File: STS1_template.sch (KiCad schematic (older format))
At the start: 10 parts, among them J1 Conn_01x02_Female, U1 coordinate_system

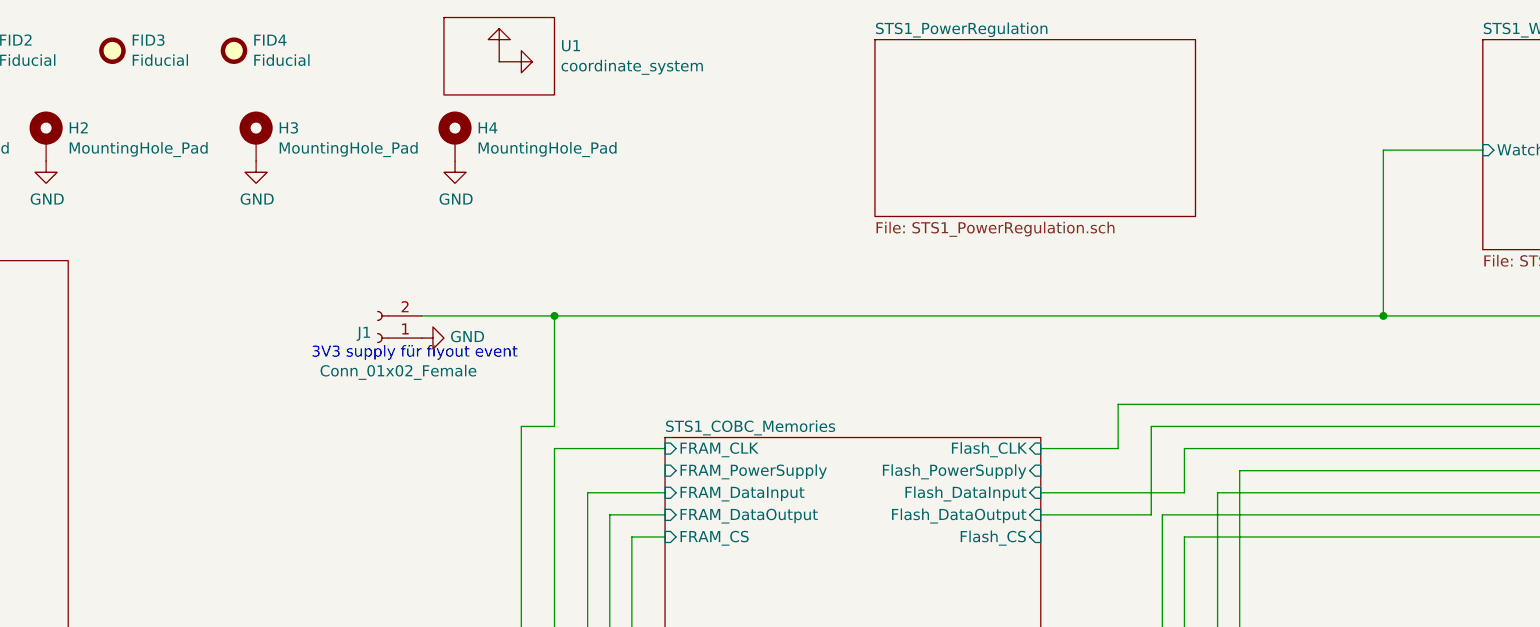
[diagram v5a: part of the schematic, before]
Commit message: BuckBoost added
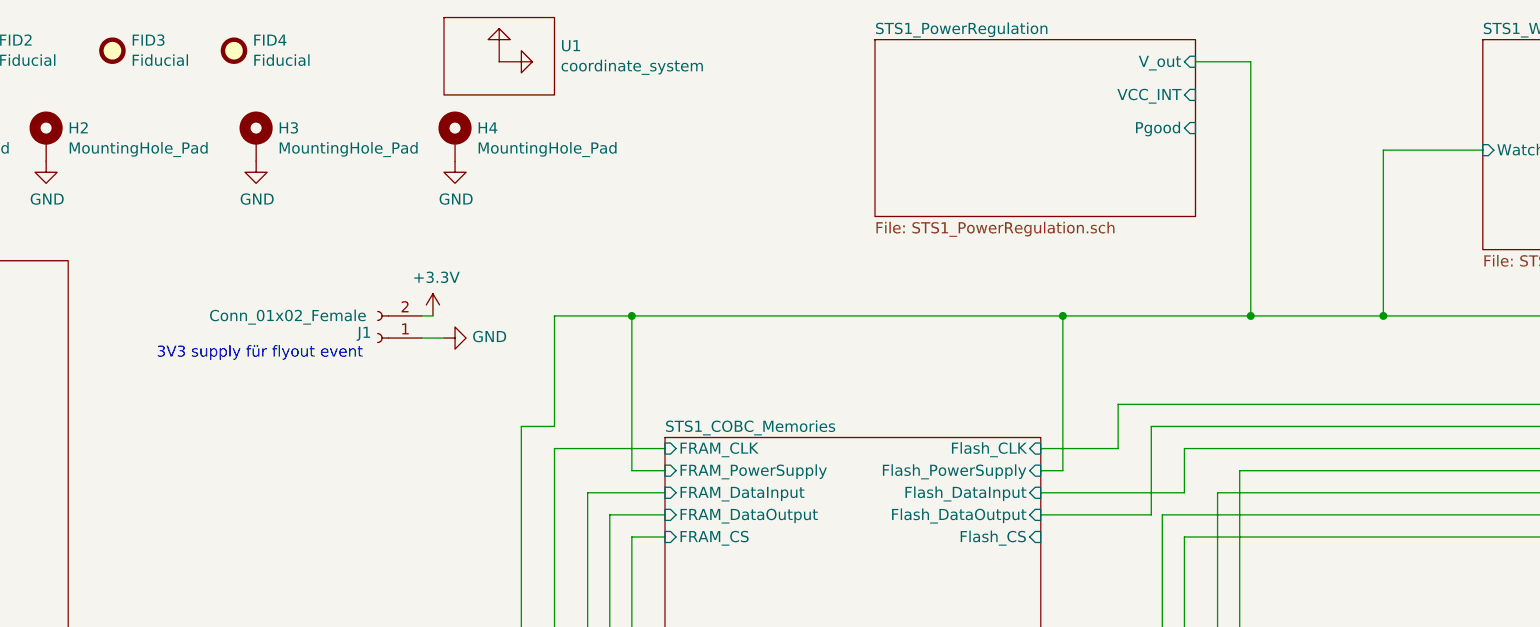
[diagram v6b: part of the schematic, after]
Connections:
- net STS1_COBC_uC/STM32_PowerSupply1 renamed +3V3
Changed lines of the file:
@@
 F5 "Flash_DataOutput" I R 6100 2800 50
 F6 "Flash_CS" I R 6100 2900 50
-F7 "FRAM_CS" I L 4400 2900 50
-F8 "FRAM_CLK" I L 4400 2500 50
-F9 "FRAM_DataInput" I L 4400 2700 50
-F10 "FRAM_DataOutput" I L 4400 2800 50
-F11 "FRAM_PowerSupply" I L 4400 2600 50
+F7 "FRAM_CLK" I L 4400 2500 50
+F8 "FRAM_DataInput" I L 4400 2700 50
+F9 "FRAM_DataOutput" I L 4400 2800 50
+F10 "FRAM_PowerSupply" I L 4400 2600 50
+F11 "FRAM_CS" I L 4400 2900 50
 $EndSheet
 Wire Wire Line
@@
 	8950 2900 6750 2900
 Wire Wire Line
-	6750 2900 6750 3900
-Wire Wire Line
 	6750 3900 3900 3900
 Wire Wire Line
@@
 Wire Wire Line
 	8950 2700 6900 2700
-Wire Wire Line
-	6900 2700 6900 3700
 Wire Wire Line
 	6900 3700 4150 3700
@@
 F0 "STS1_PowerRegulation" 50
 F1 "STS1_PowerRegulation.sch" 50
+F2 "V_out" I R 6800 750 50
+F3 "VCC_INT" I R 6800 900 50
+F4 "Pgood" I R 6800 1050 50
 $EndSheet
 $Sheet
@@
 P 3100 2000
 F 0 "J1" H 3128 1976 50  0000 L CNN
-F 1 "Conn_01x02_Female" H 2650 2150 50  0000 L CNN
+F 1 "Conn_01x02_Female" H 3150 1900 50  0000 L CNN
 F 2 "Connector_PinHeader_2.54mm:PinHeader_1x02_P2.54mm_Vertical" H 3100 2000 50  0001 C CNN
 F 3 "~" H 3100 2000 50  0001 C CNN
@@
 	-1   0    0    1
 $EndComp
-Text Notes 2800 2100 0    50   ~ 0
+Text Notes 2100 2100 0    50   ~ 0
 3V3 supply für flyout event\n
 Wire Wire Line
-	3300 1900 3900 1900
+	3300 1900 3350 1900
 Wire Wire Line
 	8600 1900 8600 3100
@@
 L power:GND #PWR0123
 U 1 1 612FF8A3
-P 3300 2000
-F 0 "#PWR0123" H 3300 1750 50  0001 C CNN
-F 1 "GND" V 3305 1872 50  0000 R CNN
-F 2 "" H 3300 2000 50  0001 C CNN
-F 3 "" H 3300 2000 50  0001 C CNN
-	1    3300 2000
+P 3400 2000
+F 0 "#PWR0123" H 3400 1750 50  0001 C CNN
+F 1 "GND" V 3405 1872 50  0000 R CNN
+F 2 "" H 3400 2000 50  0001 C CNN
+F 3 "" H 3400 2000 50  0001 C CNN
+	1    3400 2000
 	0    -1   -1   0
 $EndComp
@@
 Wire Wire Line
 	3750 6100 2600 6100
-Connection ~ 3900 1900
-Wire Wire Line
-	3900 1900 7650 1900
 Wire Wire Line
 	3750 5900 550  5900
@@
 	8950 2600 7000 2600
 Wire Wire Line
-	7000 2600 7000 3600
-Wire Wire Line
 	7000 3600 4250 3600
 Wire Wire Line
@@
 Wire Wire Line
 	10400 1050 10100 1050
+Wire Wire Line
+	7000 2600 7000 3600
+Wire Wire Line
+	6900 2700 6900 3700
+Wire Wire Line
+	6750 2900 6750 3900
+$Comp
+L power:+3.3V #PWR0157
+U 1 1 615E09EC
+P 3350 1900
+F 0 "#PWR0157" H 3350 1750 50  0001 C CNN
+F 1 "+3.3V" H 3365 2073 50  0000 C CNN
+F 2 "" H 3350 1900 50  0001 C CNN
+F 3 "" H 3350 1900 50  0001 C CNN
+	1    3350 1900
+	1    0    0    -1
+$EndComp
+Wire Wire Line
+	3300 2000 3400 2000
+Wire Wire Line
+	6800 750  7050 750
+Wire Wire Line
+	7050 750  7050 1900
+Connection ~ 7050 1900
+Wire Wire Line
+	7050 1900 7650 1900
+Wire Wire Line
+	4400 2600 4250 2600
+Wire Wire Line
+	4250 2600 4250 1900
+Wire Wire Line
+	3900 1900 4250 1900
+Connection ~ 4250 1900
+Wire Wire Line
+	4250 1900 6200 1900
+Wire Wire Line
+	6100 2600 6200 2600
+Wire Wire Line
+	6200 2600 6200 1900
+Connection ~ 6200 1900
+Wire Wire Line
+	6200 1900 7050 1900
 $EndSCHEMATC

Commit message: schematic done
final tweaks (adding LEDS, pin headers, moving circuits...)
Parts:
- removed J1: Conn_01x02_Female, Connector_PinHeader_2.54mm:PinHeader_1x02_P2.54mm_Vertical, symbol Connector:Conn_01x02_Female
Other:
- note removed: "3V3 supply für flyout event\n"

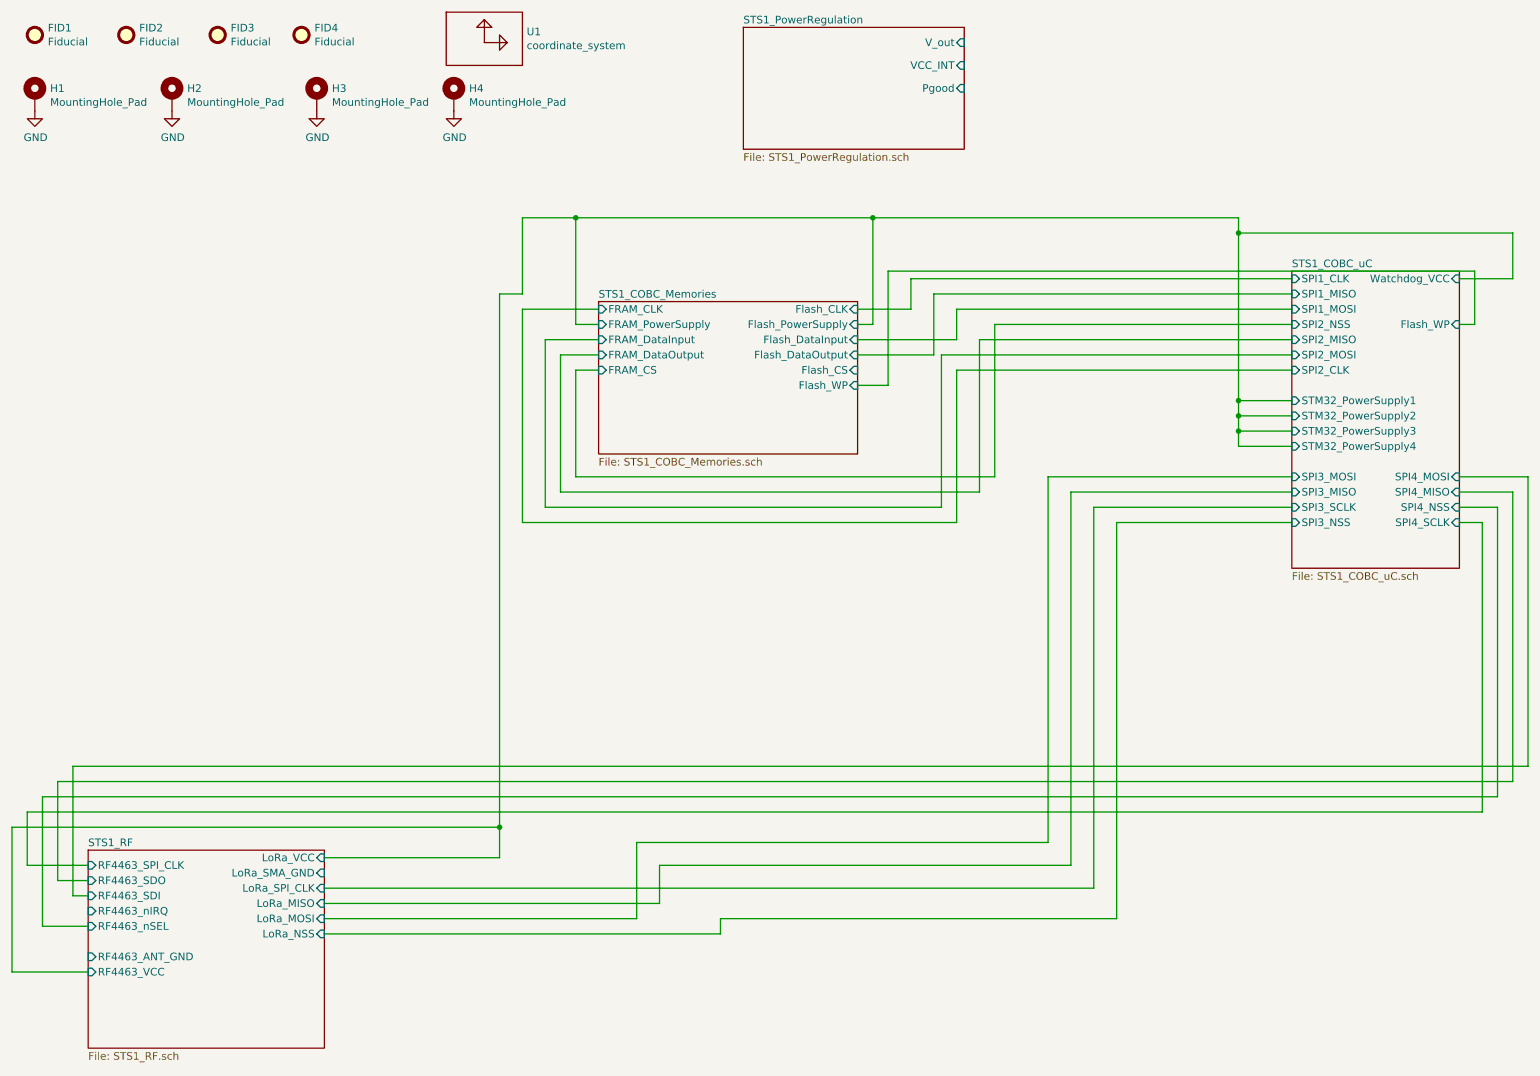
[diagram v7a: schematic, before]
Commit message: Issues removed + further layout development
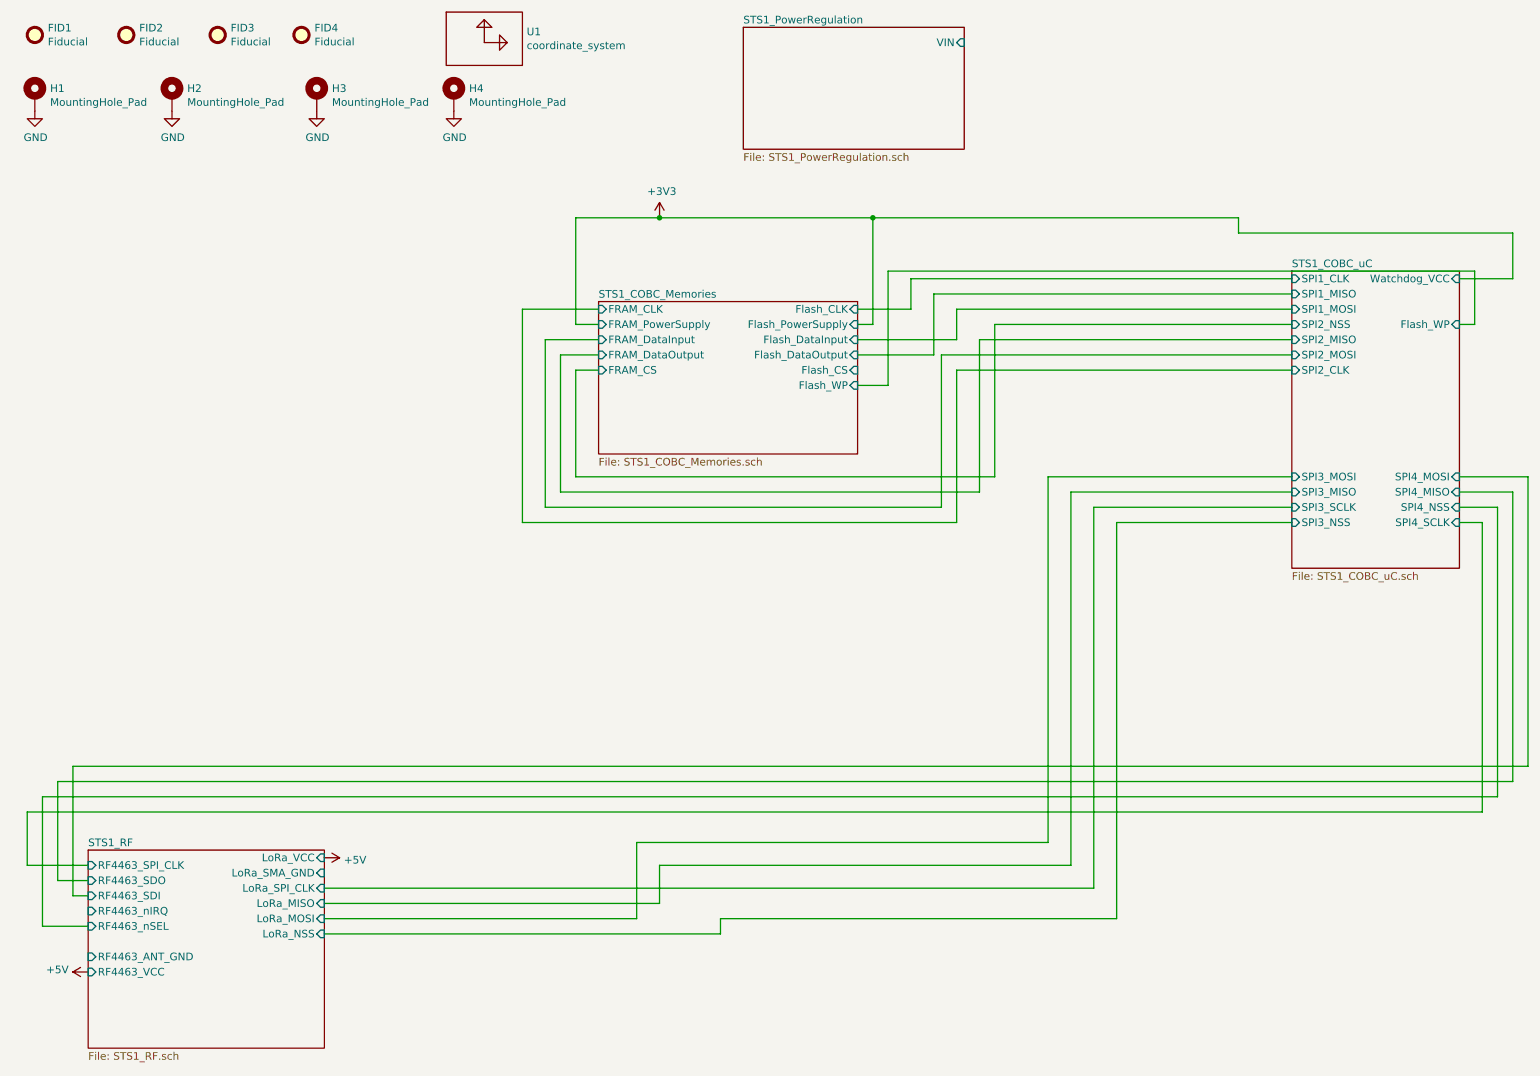
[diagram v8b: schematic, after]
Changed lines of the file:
@@
 Wire Wire Line
 	4150 2800 4400 2800
-$Sheet
-S 5350 650  1450 800
-U 61293CFB
-F0 "STS1_PowerRegulation" 50
-F1 "STS1_PowerRegulation.sch" 50
-F2 "V_out" I R 6800 750 50
-F3 "VCC_INT" I R 6800 900 50
-F4 "Pgood" I R 6800 1050 50
-$EndSheet
 Wire Wire Line
 	8600 1900 8600 2000
-Wire Wire Line
-	8600 3100 8950 3100
 $Sheet
 S 1050 6050 1550 1300
@@
 	7350 3600 8950 3600
 Wire Wire Line
-	3900 1900 3900 2400
-Wire Wire Line
-	3900 2400 3750 2400
-Wire Wire Line
-	3750 2400 3750 5900
-Wire Wire Line
-	3750 6100 2600 6100
-Wire Wire Line
-	3750 5900 550  5900
-Wire Wire Line
-	550  5900 550  6850
-Wire Wire Line
-	550  6850 1050 6850
-Connection ~ 3750 5900
-Wire Wire Line
-	3750 5900 3750 6100
-Wire Wire Line
-	8600 3100 8600 3200
-Wire Wire Line
-	8600 3200 8950 3200
-Connection ~ 8600 3100
-Wire Wire Line
-	8600 3200 8600 3300
-Wire Wire Line
-	8600 3300 8950 3300
-Connection ~ 8600 3200
-Wire Wire Line
-	8600 3300 8600 3400
-Wire Wire Line
-	8600 3400 8950 3400
-Connection ~ 8600 3300
-Wire Wire Line
 	10050 3900 10200 3900
 Wire Wire Line
@@
 	4250 2600 4250 1900
 Wire Wire Line
-	3900 1900 4250 1900
-Connection ~ 4250 1900
-Wire Wire Line
-	4250 1900 6200 1900
+	4250 1900 4800 1900
 Wire Wire Line
 	6100 2600 6200 2600
@@
 Wire Wire Line
 	6200 1900 8600 1900
+Wire Wire Line
+	10050 2300 10400 2300
+Wire Wire Line
+	10400 2300 10400 2000
+Wire Wire Line
+	10400 2000 8600 2000
 $Sheet
 S 8950 2250 1100 1950
@@
 F6 "SPI2_MOSI" I L 8950 2800 50
 F7 "SPI2_CLK" I L 8950 2900 50
-F8 "STM32_PowerSupply1" I L 8950 3100 50
-F9 "STM32_PowerSupply2" I L 8950 3200 50
-F10 "STM32_PowerSupply3" I L 8950 3300 50
-F11 "STM32_PowerSupply4" I L 8950 3400 50
-F12 "SPI3_MOSI" I L 8950 3600 50
-F13 "SPI3_MISO" I L 8950 3700 50
-F14 "SPI3_SCLK" I L 8950 3800 50
-F15 "SPI3_NSS" I L 8950 3900 50
-F16 "SPI4_MOSI" I R 10050 3600 50
-F17 "SPI4_MISO" I R 10050 3700 50
-F18 "SPI2_NSS" I L 8950 2600 50
-F19 "SPI4_NSS" I R 10050 3800 50
-F20 "SPI4_SCLK" I R 10050 3900 50
-F21 "Flash_WP" I R 10050 2600 50
-F22 "Watchdog_VCC" I R 10050 2300 50
+F8 "SPI3_MOSI" I L 8950 3600 50
+F9 "SPI3_MISO" I L 8950 3700 50
+F10 "SPI3_SCLK" I L 8950 3800 50
+F11 "SPI3_NSS" I L 8950 3900 50
+F12 "SPI4_MOSI" I R 10050 3600 50
+F13 "SPI4_MISO" I R 10050 3700 50
+F14 "SPI2_NSS" I L 8950 2600 50
+F15 "SPI4_NSS" I R 10050 3800 50
+F16 "SPI4_SCLK" I R 10050 3900 50
+F17 "Flash_WP" I R 10050 2600 50
+F18 "Watchdog_VCC" I R 10050 2300 50
 $EndSheet
-Wire Wire Line
-	10050 2300 10400 2300
-Wire Wire Line
-	10400 2300 10400 2000
-Wire Wire Line
-	10400 2000 8600 2000
-Connection ~ 8600 2000
-Wire Wire Line
-	8600 2000 8600 3100
+$Comp
+L power:+3V3 #PWR0105
+U 1 1 617A5044
+P 4800 1900
+F 0 "#PWR0105" H 4800 1750 50  0001 C CNN
+F 1 "+3V3" H 4815 2073 50  0000 C CNN
+F 2 "" H 4800 1900 50  0001 C CNN
+F 3 "" H 4800 1900 50  0001 C CNN
+	1    4800 1900
+	1    0    0    -1
+$EndComp
+Connection ~ 4800 1900
+Wire Wire Line
+	4800 1900 6200 1900
+$Sheet
+S 5350 650  1450 800
+U 61293CFB
+F0 "STS1_PowerRegulation" 50
+F1 "STS1_PowerRegulation.sch" 50
+F2 "VIN" I R 6800 750 50
+$EndSheet
+$Comp
+L power:+5V #PWR0141
+U 1 1 617B5FC9
+P 2600 6100
+F 0 "#PWR0141" H 2600 5950 50  0001 C CNN
+F 1 "+5V" V 2615 6228 50  0000 L CNN
+F 2 "" H 2600 6100 50  0001 C CNN
+F 3 "" H 2600 6100 50  0001 C CNN
+	1    2600 6100
+	0    1    1    0
+$EndComp
+$Comp
+L power:+5V #PWR0142
+U 1 1 617B68B0
+P 1050 6850
+F 0 "#PWR0142" H 1050 6700 50  0001 C CNN
+F 1 "+5V" V 1065 6978 50  0000 L CNN
+F 2 "" H 1050 6850 50  0001 C CNN
+F 3 "" H 1050 6850 50  0001 C CNN
+	1    1050 6850
+	0    -1   -1   0
+$EndComp
 $EndSCHEMATC
